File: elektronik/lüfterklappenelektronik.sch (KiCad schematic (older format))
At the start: 96 parts, among them J101 Conn_01x05_Male, J102 Conn_FAN, J103 Conn_LAN_ENC28J60, J104 USB_B_Micro, J105 #Stecker, P101 PWR_BUS_CONN1, P102 #FAN_230VAC_Phase, P103 PressureSensor3, P104 PressureSensor1, P105 PressureSensor2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

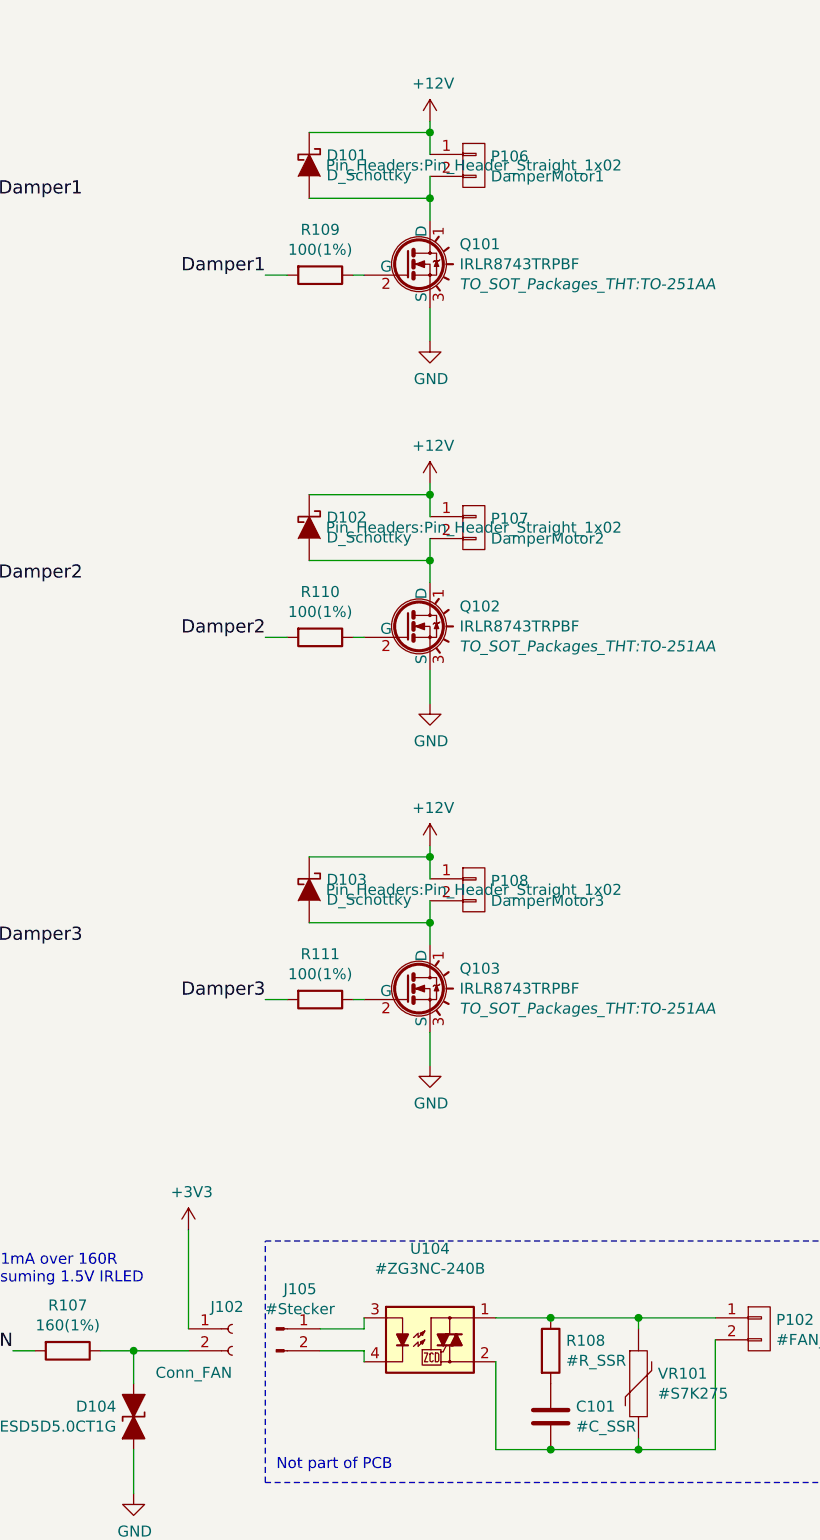
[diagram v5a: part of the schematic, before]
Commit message: fixed connectors
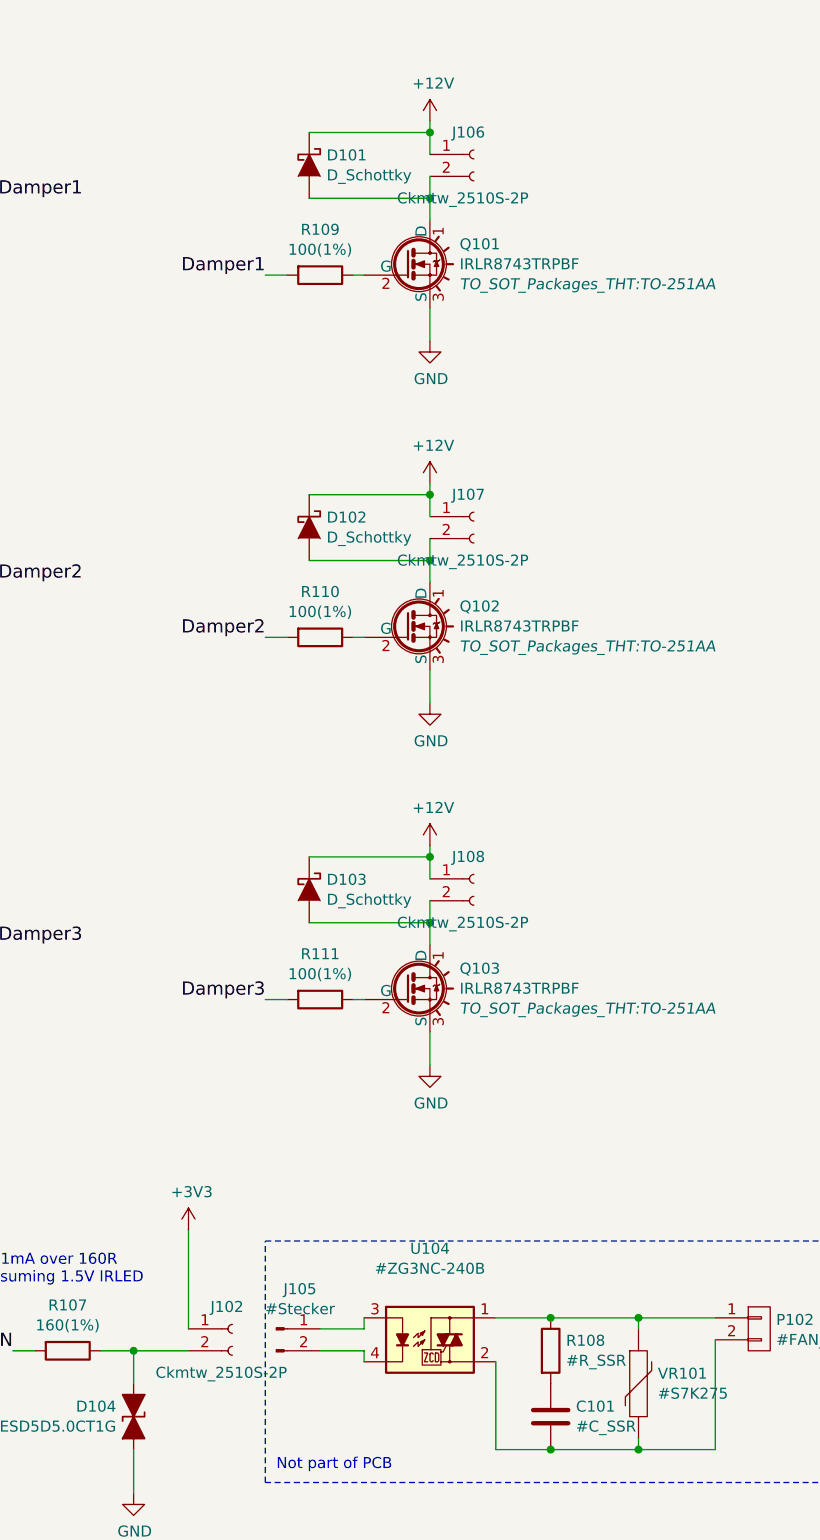
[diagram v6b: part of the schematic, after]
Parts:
- removed P106: DamperMotor1, Pin_Headers:Pin_Header_Straight_1x02, symbol lüfterklappenelektronik-rescue:CONN_01X02
- removed P107: DamperMotor2, Pin_Headers:Pin_Header_Straight_1x02, symbol lüfterklappenelektronik-rescue:CONN_01X02
- removed P108: DamperMotor3, Pin_Headers:Pin_Header_Straight_1x02, symbol lüfterklappenelektronik-rescue:CONN_01X02
- added J106, J107, J108: Ckmtw_2510S-2P, Connect:PINHEAD1-2, symbol Connector:Conn_01x02_Female
- J102: value Conn_FAN -> Ckmtw_2510S-2P
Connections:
- net +12V: now also J106.1 (Pin_1), J107.1 (Pin_1), J108.1 (Pin_1)
- net at D101.2 (A), Q101.1 (D): now also J106.2 (Pin_2)
- net at D102.2 (A), Q102.1 (D): now also J107.2 (Pin_2)
- net at D103.2 (A), Q103.1 (D): now also J108.2 (Pin_2)
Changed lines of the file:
@@
-$EndComp
-$Comp
-L lüfterklappenelektronik-rescue:CONN_01X02 P106
-U 1 1 57419C9B
-P 5150 1350
-F 0 "P106" H 5227 1391 50  0000 L CNN
-F 1 "DamperMotor1" H 5227 1300 50  0000 L CNN
-F 2 "Pin_Headers:Pin_Header_Straight_1x02" H 5150 1350 50  0000 C CNN
-F 3 "" H 5150 1350 50  0000 C CNN
-	1    5150 1350
-	1    0    0    -1
 $EndComp
 $Comp
@@
 	4200 1850 4300 1850
 $Comp
-L lüfterklappenelektronik-rescue:CONN_01X02 P107
-U 1 1 5741A884
-P 5150 3000
-F 0 "P107" H 5227 3041 50  0000 L CNN
-F 1 "DamperMotor2" H 5227 2950 50  0000 L CNN
-F 2 "Pin_Headers:Pin_Header_Straight_1x02" H 5150 3000 50  0000 C CNN
-F 3 "" H 5150 3000 50  0000 C CNN
-	1    5150 3000
-	1    0    0    -1
-$EndComp
-$Comp
 L power:+12V #PWR03
 U 1 1 5741A88A
@@
 Wire Wire Line
 	4200 3500 4300 3500
-$Comp
-L lüfterklappenelektronik-rescue:CONN_01X02 P108
-U 1 1 5741AA32
-P 5150 4650
-F 0 "P108" H 5227 4691 50  0000 L CNN
-F 1 "DamperMotor3" H 5227 4600 50  0000 L CNN
-F 2 "Pin_Headers:Pin_Header_Straight_1x02" H 5150 4650 50  0000 C CNN
-F 3 "" H 5150 4650 50  0000 C CNN
-	1    5150 4650
-	1    0    0    -1
-$EndComp
 $Comp
 L power:+12V #PWR05
@@
 P 4050 6650
 F 0 "J102" H 3950 6750 50  0000 L CNN
-F 1 "Conn_FAN" H 3700 6450 50  0000 L CNN
+F 1 "Ckmtw_2510S-2P" H 3700 6450 50  0000 L CNN
 F 2 "Connect:PINHEAD1-2" H 4050 6650 50  0001 C CNN
 F 3 "~" H 4050 6650 50  0001 C CNN
@@
 	1    0    0    -1
 $EndComp
+$Comp
+L Connector:Conn_01x02_Female J106
+U 1 1 60F95904
+P 5150 1300
+F 0 "J106" H 5050 1400 50  0000 L CNN
+F 1 "Ckmtw_2510S-2P" H 4800 1100 50  0000 L CNN
+F 2 "Connect:PINHEAD1-2" H 5150 1300 50  0001 C CNN
+F 3 "~" H 5150 1300 50  0001 C CNN
+F 4 " BOOMELE(Boom Precision Elec) " H 5150 1300 50  0001 C CNN "MF"
+F 5 "C30436" H 5150 1300 50  0001 C CNN "MP"
+F 6 "LCSC" H 5150 1300 50  0001 C CNN "Distributor"
+F 7 "C30436" H 5150 1300 50  0001 C CNN "LCSCPartN"
+	1    5150 1300
+	1    0    0    -1
+$EndComp
+$Comp
+L Connector:Conn_01x02_Female J107
+U 1 1 60FA2504
+P 5150 2950
+F 0 "J107" H 5050 3050 50  0000 L CNN
+F 1 "Ckmtw_2510S-2P" H 4800 2750 50  0000 L CNN
+F 2 "Connect:PINHEAD1-2" H 5150 2950 50  0001 C CNN
+F 3 "~" H 5150 2950 50  0001 C CNN
+F 4 " BOOMELE(Boom Precision Elec) " H 5150 2950 50  0001 C CNN "MF"
+F 5 "C30436" H 5150 2950 50  0001 C CNN "MP"
+F 6 "LCSC" H 5150 2950 50  0001 C CNN "Distributor"
+F 7 "C30436" H 5150 2950 50  0001 C CNN "LCSCPartN"
+	1    5150 2950
+	1    0    0    -1
+$EndComp
+$Comp
+L Connector:Conn_01x02_Female J108
+U 1 1 60FA3064
+P 5150 4600
+F 0 "J108" H 5050 4700 50  0000 L CNN
+F 1 "Ckmtw_2510S-2P" H 4800 4400 50  0000 L CNN
+F 2 "Connect:PINHEAD1-2" H 5150 4600 50  0001 C CNN
+F 3 "~" H 5150 4600 50  0001 C CNN
+F 4 " BOOMELE(Boom Precision Elec) " H 5150 4600 50  0001 C CNN "MF"
+F 5 "C30436" H 5150 4600 50  0001 C CNN "MP"
+F 6 "LCSC" H 5150 4600 50  0001 C CNN "Distributor"
+F 7 "C30436" H 5150 4600 50  0001 C CNN "LCSCPartN"
+	1    5150 4600
+	1    0    0    -1
+$EndComp

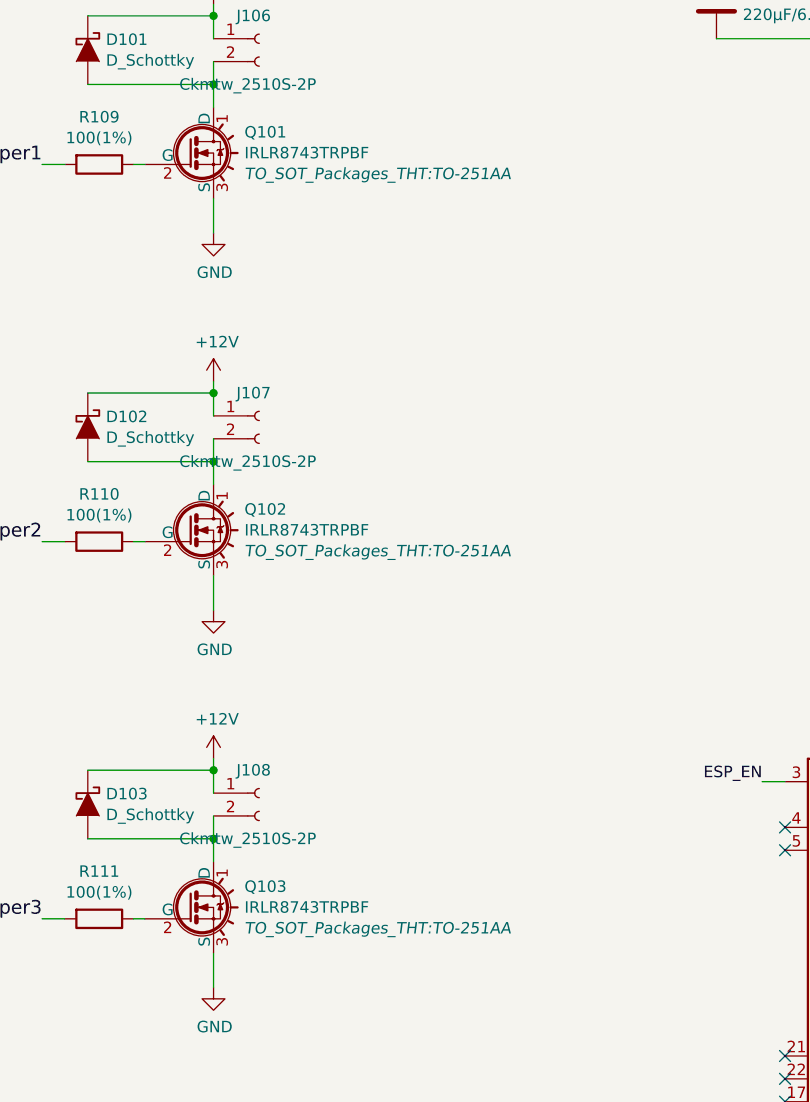
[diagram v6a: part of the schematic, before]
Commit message: fixed footprints of R and Diode
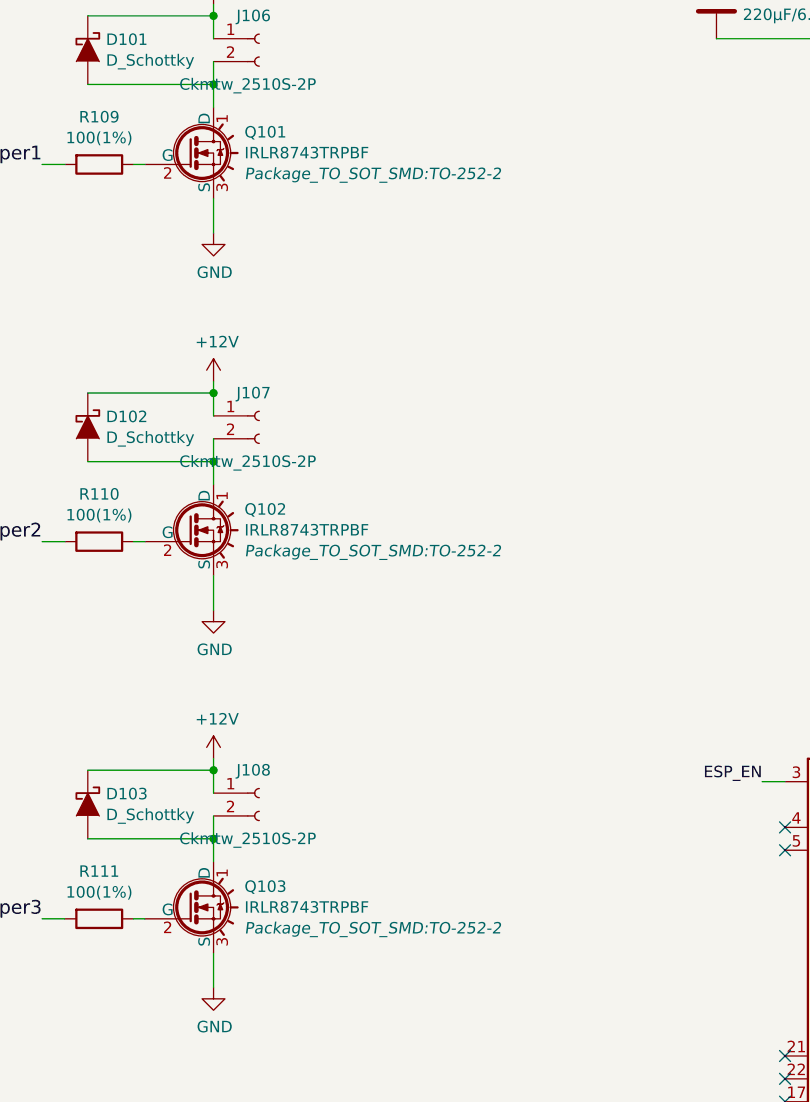
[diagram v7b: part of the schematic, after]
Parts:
- D106, D107, D108, D115: footprint Diode_THT:D_DO-35_SOD27_P7.62mm_Horizontal -> Diode_SMD:D_SOD-323
- Q101, Q102, Q103: footprint TO_SOT_Packages_THT:TO-251AA -> Package_TO_SOT_SMD:TO-252-2
- R101, R102, R103, R104, R105, R106, R107: footprint Resistors_ThroughHole:Resistor_Horizontal_RM7mm -> Resistor_SMD:R_0603_1608Metric
- R109, R110, R111: footprint Resistors_SMD:R_0603 -> Resistor_SMD:R_0603_1608Metric
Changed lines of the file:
@@
 F 0 "R109" V 4243 1850 50  0000 C CNN
 F 1 "100(1%)" V 4334 1850 50  0000 C CNN
-F 2 "Resistors_SMD:R_0603" V 4380 1850 50  0001 C CNN
+F 2 "Resistor_SMD:R_0603_1608Metric" V 4380 1850 50  0001 C CNN
 F 3 "" H 4450 1850 50  0000 C CNN
 	1    4450 1850
@@
 F 0 "R110" V 4243 3500 50  0000 C CNN
 F 1 "100(1%)" V 4334 3500 50  0000 C CNN
-F 2 "Resistors_SMD:R_0603" V 4380 3500 50  0001 C CNN
+F 2 "Resistor_SMD:R_0603_1608Metric" V 4380 3500 50  0001 C CNN
 F 3 "" H 4450 3500 50  0000 C CNN
 	1    4450 3500
@@
 F 0 "R111" V 4243 5150 50  0000 C CNN
 F 1 "100(1%)" V 4334 5150 50  0000 C CNN
-F 2 "Resistors_SMD:R_0603" V 4380 5150 50  0001 C CNN
+F 2 "Resistor_SMD:R_0603_1608Metric" V 4380 5150 50  0001 C CNN
 F 3 "" H 4450 5150 50  0000 C CNN
 	1    4450 5150
@@
 F 0 "R107" V 3093 6750 50  0000 C CNN
 F 1 "160(1%)" V 3184 6750 50  0000 C CNN
-F 2 "Resistors_ThroughHole:Resistor_Horizontal_RM7mm" V 3230 6750 50  0001 C CNN
+F 2 "Resistor_SMD:R_0603_1608Metric" V 3230 6750 50  0001 C CNN
 F 3 "" H 3300 6750 50  0000 C CNN
 	1    3300 6750
@@
 F 0 "R101" H 1220 1246 50  0000 L CNN
 F 1 "43(1%)" H 1220 1155 50  0000 L CNN
-F 2 "Resistors_ThroughHole:Resistor_Horizontal_RM7mm" V 1080 1200 50  0001 C CNN
+F 2 "Resistor_SMD:R_0603_1608Metric" V 1080 1200 50  0001 C CNN
 F 3 "" H 1150 1200 50  0000 C CNN
 	1    1150 1200
@@
 F 0 "R104" H 2420 2096 50  0000 L CNN
 F 1 "2K2" H 2420 2005 50  0000 L CNN
-F 2 "Resistors_ThroughHole:Resistor_Horizontal_RM7mm" V 2280 2050 50  0001 C CNN
+F 2 "Resistor_SMD:R_0603_1608Metric" V 2280 2050 50  0001 C CNN
 F 3 "" H 2350 2050 50  0000 C CNN
 	1    2350 2050
@@
 F 0 "R102" H 1220 2996 50  0000 L CNN
 F 1 "43(1%)" H 1220 2905 50  0000 L CNN
-F 2 "Resistors_ThroughHole:Resistor_Horizontal_RM7mm" V 1080 2950 50  0001 C CNN
+F 2 "Resistor_SMD:R_0603_1608Metric" V 1080 2950 50  0001 C CNN
 F 3 "" H 1150 2950 50  0000 C CNN
 	1    1150 2950
@@
 F 0 "R105" H 2420 3846 50  0000 L CNN
 F 1 "2K2" H 2420 3755 50  0000 L CNN
-F 2 "Resistors_ThroughHole:Resistor_Horizontal_RM7mm" V 2280 3800 50  0001 C CNN
+F 2 "Resistor_SMD:R_0603_1608Metric" V 2280 3800 50  0001 C CNN
 F 3 "" H 2350 3800 50  0000 C CNN
 	1    2350 3800
@@
 F 0 "R103" H 1220 4646 50  0000 L CNN
 F 1 "43(1%)" H 1220 4555 50  0000 L CNN
-F 2 "Resistors_ThroughHole:Resistor_Horizontal_RM7mm" V 1080 4600 50  0001 C CNN
+F 2 "Resistor_SMD:R_0603_1608Metric" V 1080 4600 50  0001 C CNN
 F 3 "" H 1150 4600 50  0000 C CNN
 	1    1150 4600
@@
 F 0 "R106" H 2420 5496 50  0000 L CNN
 F 1 "2K2" H 2420 5405 50  0000 L CNN
-F 2 "Resistors_ThroughHole:Resistor_Horizontal_RM7mm" V 2280 5450 50  0001 C CNN
+F 2 "Resistor_SMD:R_0603_1608Metric" V 2280 5450 50  0001 C CNN
 F 3 "" H 2350 5450 50  0000 C CNN
 	1    2350 5450
@@
 F 0 "Q103" H 5085 5191 50  0000 L CNN
 F 1 "IRLR8743TRPBF" H 5085 5100 50  0000 L CNN
-F 2 "TO_SOT_Packages_THT:TO-251AA" H 5085 5009 50  0000 L CIN
+F 2 "Package_TO_SOT_SMD:TO-252-2" H 5085 5009 50  0000 L CIN
 F 3 "" H 4850 5100 50  0000 L CNN
 	1    4850 5100
@@
 F 0 "Q102" H 5085 3541 50  0000 L CNN
 F 1 "IRLR8743TRPBF" H 5085 3450 50  0000 L CNN
-F 2 "TO_SOT_Packages_THT:TO-251AA" H 5085 3359 50  0000 L CIN
+F 2 "Package_TO_SOT_SMD:TO-252-2" H 5085 3359 50  0000 L CIN
 F 3 "" H 4850 3450 50  0000 L CNN
 	1    4850 3450
@@
 F 0 "Q101" H 5085 1891 50  0000 L CNN
 F 1 "IRLR8743TRPBF" H 5085 1800 50  0000 L CNN
-F 2 "TO_SOT_Packages_THT:TO-251AA" H 5085 1709 50  0000 L CIN
+F 2 "Package_TO_SOT_SMD:TO-252-2" H 5085 1709 50  0000 L CIN
 F 3 "https://datasheet.lcsc.com/szlcsc/1809061832_Infineon-Technologies-IRLR8743TRPBF_C51360.pdf" H 4850 1800 50  0001 L CNN
 F 4 "Infineon Technologies" H 4850 1800 50  0001 C CNN "MF"
@@
 F 0 "D115" H 11600 3484 50  0000 C CNN
 F 1 "BAT760-7" H 11600 3575 50  0000 C CNN
-F 2 "Diode_THT:D_DO-35_SOD27_P7.62mm_Horizontal" H 11600 3525 50  0001 C CNN
+F 2 "Diode_SMD:D_SOD-323" H 11600 3525 50  0001 C CNN
 F 3 "https://datasheet.lcsc.com/szlcsc/1811081720_Diodes-Incorporated-BAT760-7_C124187.pdf" H 11600 3700 50  0001 C CNN
 F 4 "Diodes Incorporated" H 11600 3700 50  0001 C CNN "MF"
@@
 F 0 "D106" H 2500 1284 50  0000 C CNN
 F 1 "BAT760-7" H 2500 1375 50  0000 C CNN
-F 2 "Diode_THT:D_DO-35_SOD27_P7.62mm_Horizontal" H 2500 1325 50  0001 C CNN
+F 2 "Diode_SMD:D_SOD-323" H 2500 1325 50  0001 C CNN
 F 3 "https://datasheet.lcsc.com/szlcsc/1811081720_Diodes-Incorporated-BAT760-7_C124187.pdf" H 2500 1500 50  0001 C CNN
 F 4 "Diodes Incorporated" H 2500 1500 50  0001 C CNN "MF"
@@
 F 0 "D107" H 2500 3034 50  0000 C CNN
 F 1 "BAT760-7" H 2500 3125 50  0000 C CNN
-F 2 "Diode_THT:D_DO-35_SOD27_P7.62mm_Horizontal" H 2500 3075 50  0001 C CNN
+F 2 "Diode_SMD:D_SOD-323" H 2500 3075 50  0001 C CNN
 F 3 "https://datasheet.lcsc.com/szlcsc/1811081720_Diodes-Incorporated-BAT760-7_C124187.pdf" H 2500 3250 50  0001 C CNN
 F 4 "Diodes Incorporated" H 2500 3250 50  0001 C CNN "MF"
@@
 F 0 "D108" H 2500 4684 50  0000 C CNN
 F 1 "BAT760-7" H 2500 4775 50  0000 C CNN
-F 2 "Diode_THT:D_DO-35_SOD27_P7.62mm_Horizontal" H 2500 4725 50  0001 C CNN
+F 2 "Diode_SMD:D_SOD-323" H 2500 4725 50  0001 C CNN
 F 3 "https://datasheet.lcsc.com/szlcsc/1811081720_Diodes-Incorporated-BAT760-7_C124187.pdf" H 2500 4900 50  0001 C CNN
 F 4 "Diodes Incorporated" H 2500 4900 50  0001 C CNN "MF"
